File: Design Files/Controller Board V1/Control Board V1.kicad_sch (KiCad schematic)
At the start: 0 parts

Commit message: yay(meeting 2/16/2025)
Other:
- sheet IO ports: added 24_IN_PMM, 24_OUT, 5V, CAP_GND, CAP_IN, GND_IN_PMM, GND_OUT, SIG_GND; removed none
- sheet LMG5200 ports: added ADC_Neg, ADC_Pos; removed ADC1, ADC2, ADC3
- sheet Pico ports: added GPIO_0, GPIO_1, GPIO_2, GPIO_3, GPIO_4, GPIO_5, I2C_Current_SCL, I2C_Current_SDA, I2C_TypeC_SCL, I2C_TypeC_SDA, LED0, LED1, LED2, LED3, LED4, LED5, LED6, LED7, PWM_bottom, PWM_top, SPI_ADC_0, SPI_ADC_1, SPI_ADC_2, buffer, inv, sig_gnd; removed SCL, SDA

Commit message: Major Schematic Progress
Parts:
- added R16, R17: 0, Resistor_SMD:R_0603_1608Metric, symbol Device:R
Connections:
- new net A_GND: R17.2
- new net D_GND: R16.1
- new net P_GND: R16.2, R17.1
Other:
- sheet 5V_PSU ports: added D_GND, IOUT, P_GND; removed GND, IOUT(5V)
- sheet IO ports: added 24V_OUT, D_GND, GPIO_0, GPIO_1, GPIO_2, GPIO_3, GPIO_4, GPIO_5, I2C_TypeC_SCL, I2C_TypeC_SDA, P_GND; removed 24_OUT, CAP_GND, GND_OUT, SIG_GND
- sheet LMG5200 ports: added D_GND, P_GND, cap_volt, cap_volt_pico_adc, high_side_FET; removed ADC_Neg, ADC_Pos, bottom_out, sig-gnd, to_xt30_capBank

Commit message: here we go agane
Updating footprints and tackling general layout
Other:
- sheet Pico ports: added ADC_0, ADC_1, ADC_2; removed none
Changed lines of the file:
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@@
+			)
+		)
+		(pin "ADC_1" output
+			(at 177.8 55.88 0)
+			(effects
+				(font
+					(size 1.27 1.27)
+				)
+				(justify right)
+			)
+		)
+		(pin "ADC_0" output
+			(at 177.8 53.34 0)
+			(effects
+				(font
+					(size 1.27 1.27)
+				)
+				(justify right)
+			)
+		)
+		(pin "ADC_2" output
+			(at 177.8 58.42 0)
+			(effects
+				(font
+					(size 1.27 1.27)
+				)
+				(justify right)
 			)
 		)

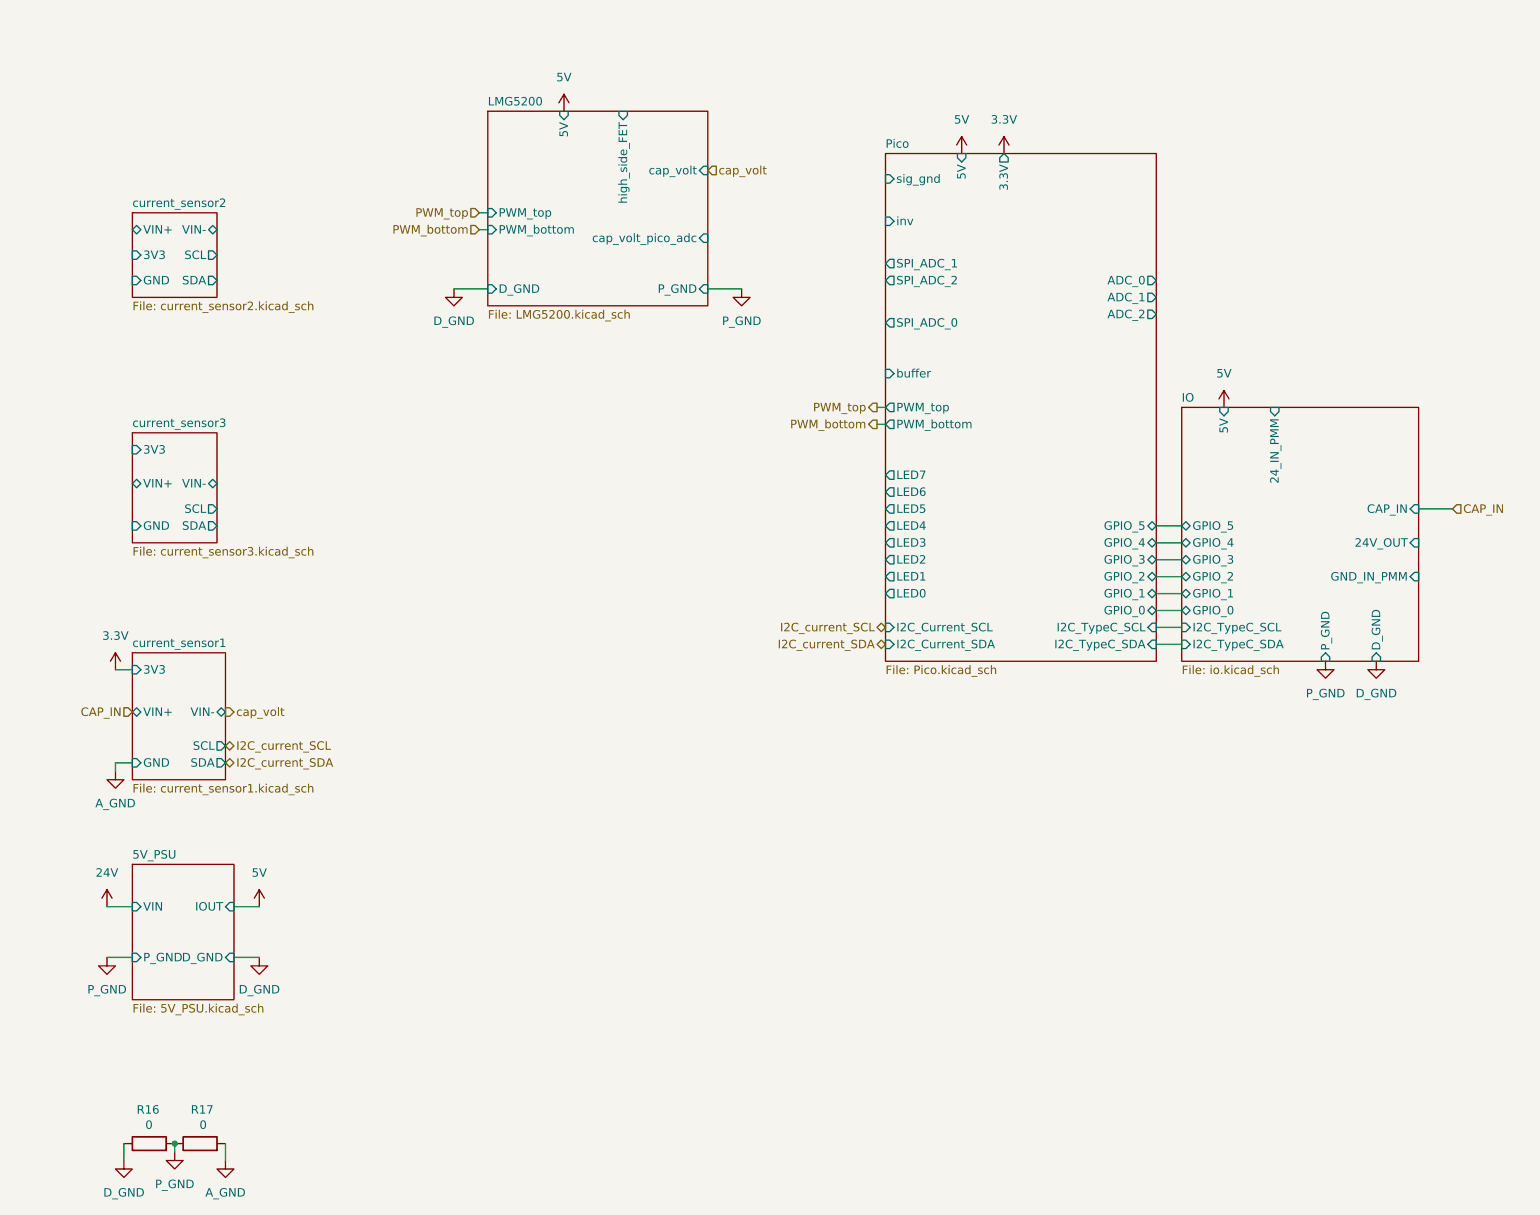
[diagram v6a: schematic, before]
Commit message: current sensor done
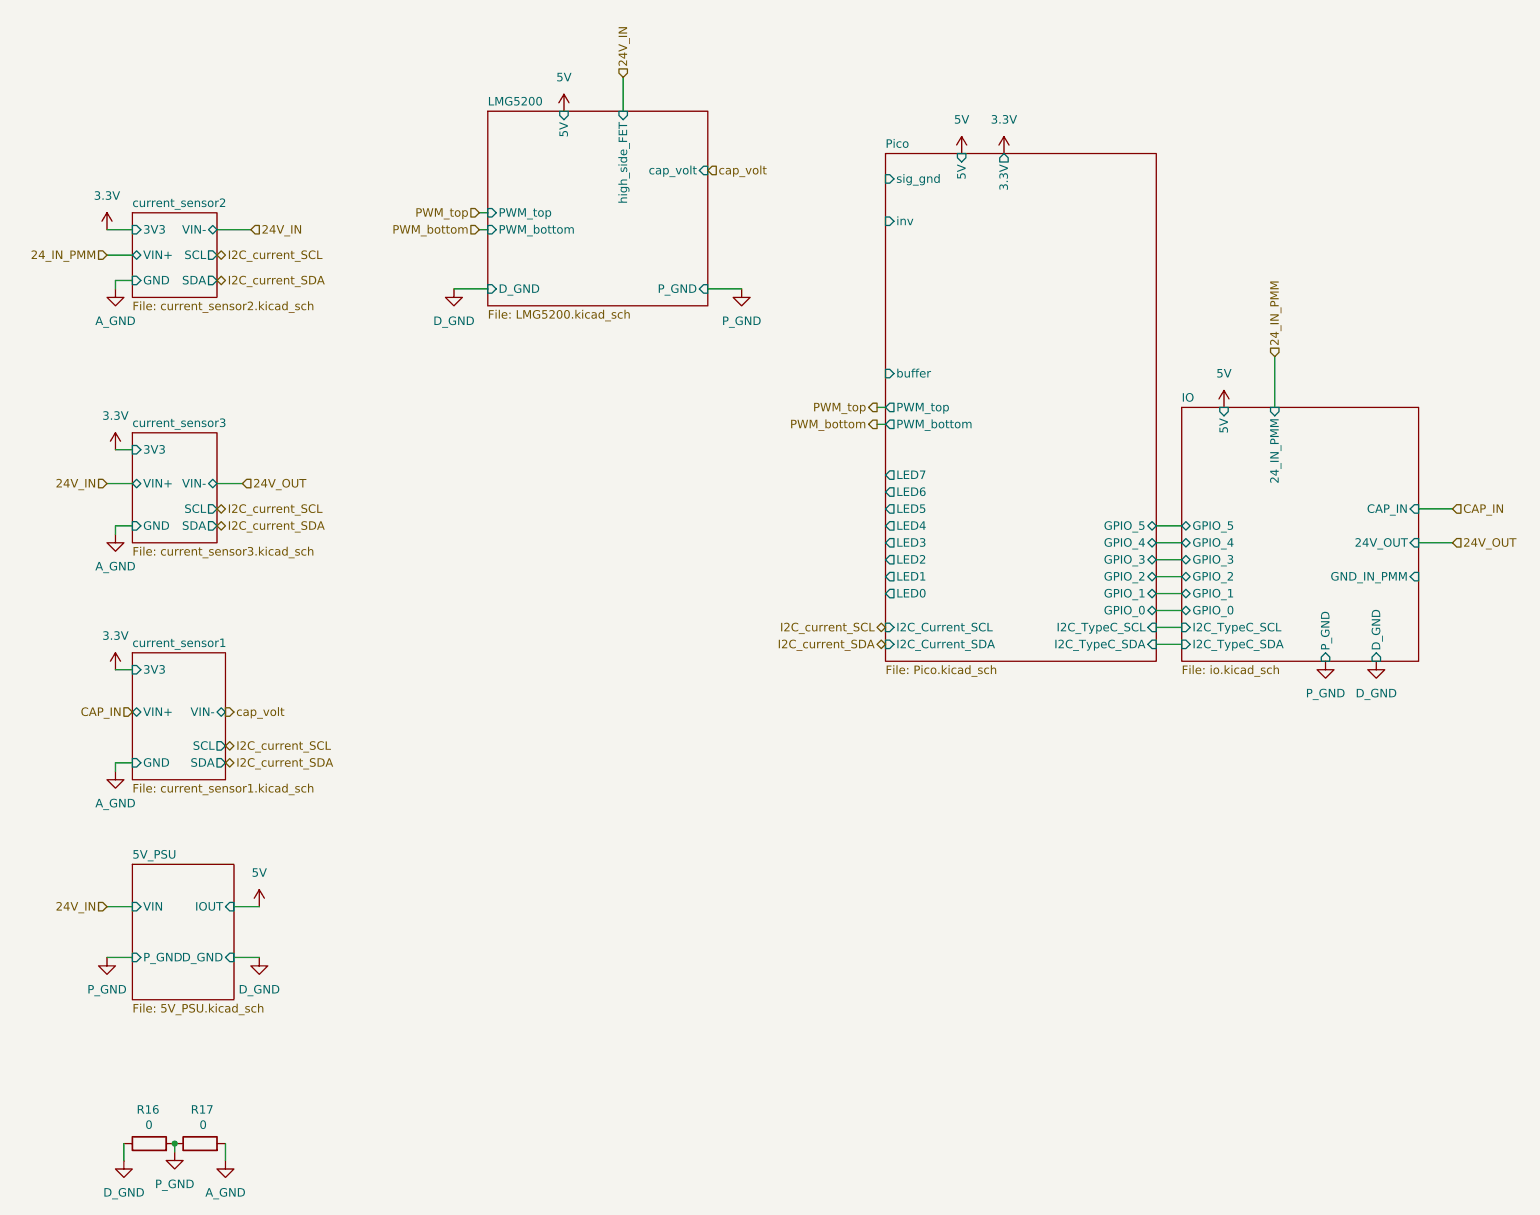
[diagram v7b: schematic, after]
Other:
- sheet LMG5200 ports: added none; removed cap_volt_pico_adc
- sheet Pico ports: added none; removed ADC_0, ADC_1, ADC_2, SPI_ADC_0, SPI_ADC_1, SPI_ADC_2

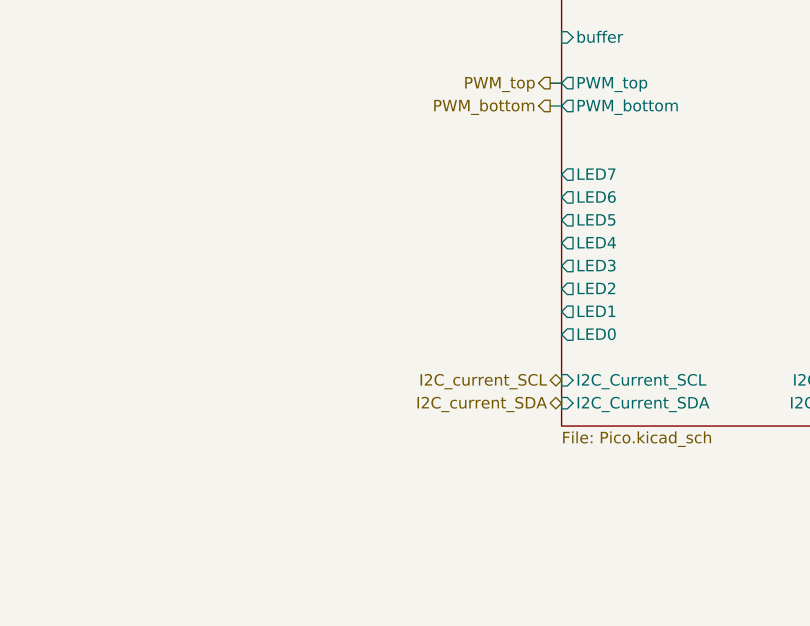
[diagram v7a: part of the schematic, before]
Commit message: Added Cap footprint, added LED, added Resistors
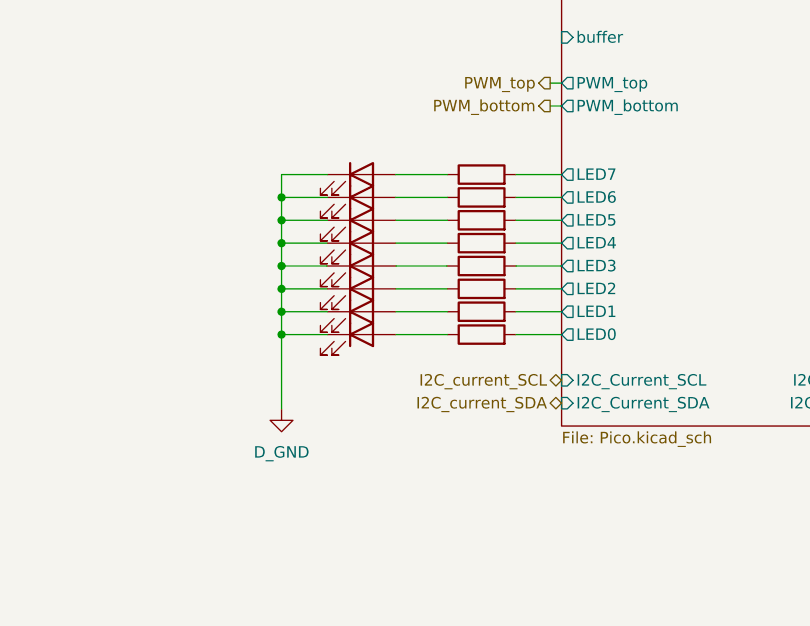
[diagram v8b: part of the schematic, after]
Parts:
- added D1, D2, D3, D4, D5, D6, D7, D8: LED, LED_SMD:LED_0603_1608Metric, symbol Device:LED
- added R1, R15, R18, R19, R20, R21, R22, R23: R, LED_SMD:LED_0805_2012Metric, symbol Device:R
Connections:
- net D_GND: now also D1.1 (K), D2.1 (K), D3.1 (K), D4.1 (K), D5.1 (K), D6.1 (K), D7.1 (K), D8.1 (K)
- net Pico/LED0: now also R1.2
- net Pico/LED1: now also R15.2
- net Pico/LED2: now also R18.2
- net Pico/LED3: now also R19.2
- net Pico/LED4: now also R20.2
- net Pico/LED5: now also R21.2
- net Pico/LED6: now also R22.2
- net Pico/LED7: now also R23.2
- new net: D4.2 (A), R19.1
- new net: D1.2 (A), R15.1
- new net: D3.2 (A), R18.1
- new net: D2.2 (A), R1.1
- new net: D7.2 (A), R22.1
- new net: D5.2 (A), R20.1
- new net: D8.2 (A), R23.1
- new net: D6.2 (A), R21.1
